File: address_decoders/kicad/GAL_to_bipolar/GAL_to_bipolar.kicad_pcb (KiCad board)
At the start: 2 copper layers, 15.2 x 28.6 mm, 2 parts, among them J1 EPROM, J2 GAL

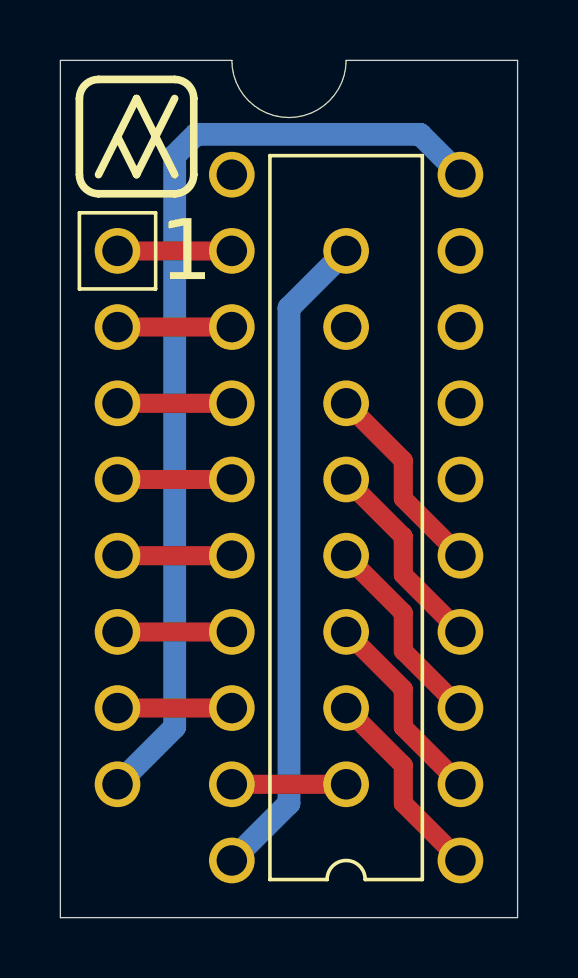
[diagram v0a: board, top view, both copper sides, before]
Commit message: Fixed the reversed address bits in the GAL adapter PCB
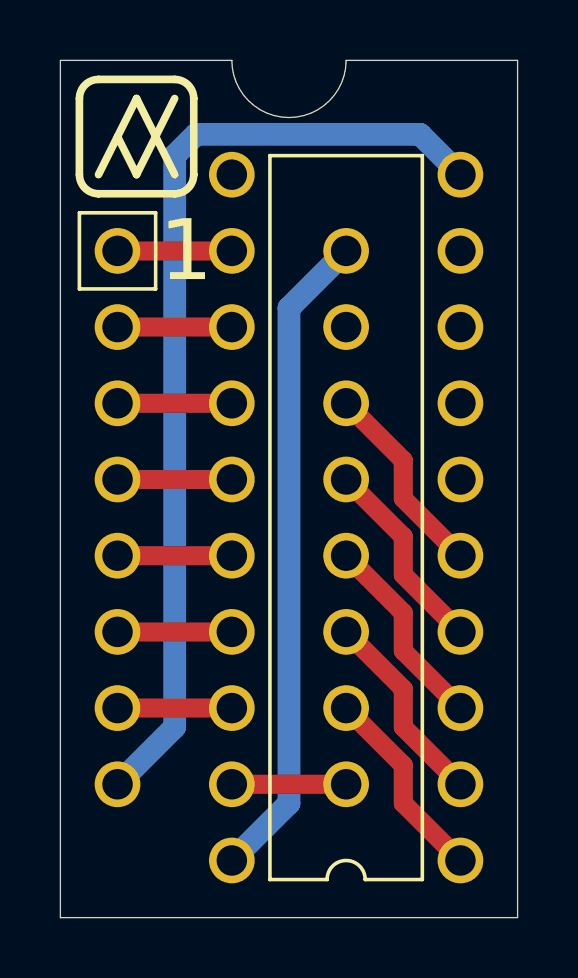
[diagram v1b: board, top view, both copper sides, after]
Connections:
- J1 pad 10: A4 -> A0
- J1 pad 11: A3 -> A1
- J1 pad 13: A1 -> A3
- J1 pad 14: A0 -> A4
- J2 pad 1: A4 -> A0
- J2 pad 2: A3 -> A1
- J2 pad 4: A1 -> A3
- J2 pad 5: A0 -> A4
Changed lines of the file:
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@@
     (fp_arc (start 0.635 -12.065) (mid 0 -11.43) (end -0.635 -12.065) (layer "F.SilkS") (width 0.12))
     (pad "1" thru_hole circle (at -3.81 -11.43 180) (size 1.524 1.524) (drill 1.016) (layers *.Cu *.Mask)
-      (net 10 "A4") (pinfunction "IO0") (pintype "bidirectional"))
+      (net 14 "A0") (pinfunction "IO0") (pintype "bidirectional"))
     (pad "2" thru_hole circle (at -3.81 -8.89 180) (size 1.524 1.524) (drill 1.016) (layers *.Cu *.Mask)
-      (net 11 "A3") (pinfunction "IO1") (pintype "bidirectional"))
+      (net 13 "A1") (pinfunction "IO1") (pintype "bidirectional"))
     (pad "3" thru_hole circle (at -3.81 -6.35 180) (size 1.524 1.524) (drill 1.016) (layers *.Cu *.Mask)
       (net 12 "A2") (pinfunction "IO2") (pintype "bidirectional"))
     (pad "4" thru_hole circle (at -3.81 -3.81 180) (size 1.524 1.524) (drill 1.016) (layers *.Cu *.Mask)
-      (net 13 "A1") (pinfunction "IO3") (pintype "bidirectional"))
+      (net 11 "A3") (pinfunction "IO3") (pintype "bidirectional"))
     (pad "5" thru_hole circle (at -3.81 -1.27 180) (size 1.524 1.524) (drill 1.016) (layers *.Cu *.Mask)
-      (net 14 "A0") (pinfunction "IO4") (pintype "bidirectional"))
+      (net 10 "A4") (pinfunction "IO4") (pintype "bidirectional"))
     (pad "6" thru_hole circle (at -3.81 1.27 180) (size 1.524 1.524) (drill 1.016) (layers *.Cu *.Mask)
       (net 17 "unconnected-(J2-Pad6)") (pinfunction "IO5") (pintype "bidirectional+no_connect"))
@@
       (net 9 "B7") (pinfunction "B7") (pintype "output"))
     (pad "10" thru_hole circle (at 3.81 6.35) (size 1.524 1.524) (drill 1.016) (layers *.Cu *.Mask)
-      (net 10 "A4") (pinfunction "A0") (pintype "input"))
+      (net 14 "A0") (pinfunction "A0") (pintype "input"))
     (pad "11" thru_hole circle (at 3.81 3.81) (size 1.524 1.524) (drill 1.016) (layers *.Cu *.Mask)
-      (net 11 "A3") (pinfunction "A1") (pintype "input"))
+      (net 13 "A1") (pinfunction "A1") (pintype "input"))
     (pad "12" thru_hole circle (at 3.81 1.27) (size 1.524 1.524) (drill 1.016) (layers *.Cu *.Mask)
       (net 12 "A2") (pinfunction "A2") (pintype "input"))
     (pad "13" thru_hole circle (at 3.81 -1.27) (size 1.524 1.524) (drill 1.016) (layers *.Cu *.Mask)
-      (net 13 "A1") (pinfunction "A3") (pintype "input"))
+      (net 11 "A3") (pinfunction "A3") (pintype "input"))
     (pad "14" thru_hole circle (at 3.81 -3.81) (size 1.524 1.524) (drill 1.016) (layers *.Cu *.Mask)
-      (net 14 "A0") (pinfunction "A4") (pintype "input"))
+      (net 10 "A4") (pinfunction "A4") (pintype "input"))
     (pad "15" thru_hole circle (at 3.81 -6.35) (size 1.524 1.524) (drill 1.016) (layers *.Cu *.Mask)
       (net 15 "unconnected-(J1-Pad15)") (pinfunction "E") (pintype "input+no_connect"))
@@
   (gr_line (start 138.43 64.77) (end 139.065 66.04) (layer "F.SilkS") (width 0.254))
   (gr_line (start 137.16 63.5) (end 137.16 66.04) (layer "F.SilkS") (width 0.254))
-  (gr_arc (start 137.16 63.5) (mid 137.345987 63.050988) (end 137.795 62.865) (layer "F.SilkS") (width 0.254))
+  (gr_arc (start 137.16 63.5) (mid 137.345987 63.050987) (end 137.795 62.865) (layer "F.SilkS") (width 0.254))
   (gr_line (start 137.795 66.04) (end 139.065 63.5) (layer "F.SilkS") (width 0.254))
   (gr_line (start 140.335 62.865) (end 137.795 62.865) (layer "F.SilkS") (width 0.254))
-  (gr_arc (start 140.335 62.865) (mid 140.784012 63.050987) (end 140.97 63.5) (layer "F.SilkS") (width 0.254))
+  (gr_arc (start 140.335 62.865) (mid 140.784013 63.050987) (end 140.97 63.5) (layer "F.SilkS") (width 0.254))
   (gr_line (start 140.97 63.5) (end 140.969999 66.039999) (layer "F.SilkS") (width 0.254))
-  (gr_arc (start 137.795 66.675) (mid 137.345988 66.489013) (end 137.16 66.04) (layer "F.SilkS") (width 0.254))
-  (gr_arc (start 140.969999 66.039999) (mid 140.784012 66.489011) (end 140.334999 66.674999) (layer "F.SilkS") (width 0.254))
+  (gr_arc (start 137.795 66.675) (mid 137.345987 66.489013) (end 137.16 66.04) (layer "F.SilkS") (width 0.254))
+  (gr_arc (start 140.969999 66.039999) (mid 140.784012 66.489012) (end 140.334999 66.674999) (layer "F.SilkS") (width 0.254))
   (gr_line (start 137.795 66.675) (end 140.334999 66.674999) (layer "F.SilkS") (width 0.254))
   (gr_line (start 139.065 66.04) (end 140.335 63.5) (layer "F.SilkS") (width 0.254))
@@
   (segment (start 148.517489 64.697489) (end 149.86 66.04) (width 0.762) (layer "B.Cu") (net 8))
   (segment (start 146.05 86.36) (end 142.24 86.36) (width 0.635) (layer "F.Cu") (net 9))
-  (segment (start 146.05 83.82) (end 147.955 85.725) (width 0.635) (layer "F.Cu") (net 10))
-  (segment (start 147.955 85.725) (end 147.955 86.995) (width 0.635) (layer "F.Cu") (net 10))
-  (segment (start 147.955 86.995) (end 149.86 88.9) (width 0.635) (layer "F.Cu") (net 10))
-  (segment (start 147.955 84.455) (end 149.86 86.36) (width 0.635) (layer "F.Cu") (net 11))
-  (segment (start 146.05 81.28) (end 147.955 83.185) (width 0.635) (layer "F.Cu") (net 11))
-  (segment (start 147.955 83.185) (end 147.955 84.455) (width 0.635) (layer "F.Cu") (net 11))
+  (segment (start 146.05 73.66) (end 147.955 75.565) (width 0.635) (layer "F.Cu") (net 10))
+  (segment (start 147.955 75.565) (end 147.955 76.835) (width 0.635) (layer "F.Cu") (net 10))
+  (segment (start 147.955 76.835) (end 149.86 78.74) (width 0.635) (layer "F.Cu") (net 10))
+  (segment (start 147.955 78.105) (end 147.955 79.375) (width 0.635) (layer "F.Cu") (net 11))
+  (segment (start 147.955 79.375) (end 149.86 81.28) (width 0.635) (layer "F.Cu") (net 11))
+  (segment (start 146.05 76.2) (end 147.955 78.105) (width 0.635) (layer "F.Cu") (net 11))
   (segment (start 146.05 78.74) (end 147.955 80.645) (width 0.635) (layer "F.Cu") (net 12))
   (segment (start 147.955 80.645) (end 147.955 81.915) (width 0.635) (layer "F.Cu") (net 12))
   (segment (start 147.955 81.915) (end 149.86 83.82) (width 0.635) (layer "F.Cu") (net 12))
-  (segment (start 147.955 78.105) (end 147.955 79.375) (width 0.635) (layer "F.Cu") (net 13))
-  (segment (start 147.955 79.375) (end 149.86 81.28) (width 0.635) (layer "F.Cu") (net 13))
-  (segment (start 146.05 76.2) (end 147.955 78.105) (width 0.635) (layer "F.Cu") (net 13))
-  (segment (start 146.05 73.66) (end 147.955 75.565) (width 0.635) (layer "F.Cu") (net 14))
-  (segment (start 147.955 75.565) (end 147.955 76.835) (width 0.635) (layer "F.Cu") (net 14))
-  (segment (start 147.955 76.835) (end 149.86 78.74) (width 0.635) (layer "F.Cu") (net 14))
+  (segment (start 147.955 84.455) (end 149.86 86.36) (width 0.635) (layer "F.Cu") (net 13))
+  (segment (start 146.05 81.28) (end 147.955 83.185) (width 0.635) (layer "F.Cu") (net 13))
+  (segment (start 147.955 83.185) (end 147.955 84.455) (width 0.635) (layer "F.Cu") (net 13))
+  (segment (start 146.05 83.82) (end 147.955 85.725) (width 0.635) (layer "F.Cu") (net 14))
+  (segment (start 147.955 85.725) (end 147.955 86.995) (width 0.635) (layer "F.Cu") (net 14))
+  (segment (start 147.955 86.995) (end 149.86 88.9) (width 0.635) (layer "F.Cu") (net 14))
   (segment (start 144.145 86.995) (end 142.24 88.9) (width 0.762) (layer "B.Cu") (net 16))
   (segment (start 146.05 68.58) (end 144.145 70.485) (width 0.762) (layer "B.Cu") (net 16))
